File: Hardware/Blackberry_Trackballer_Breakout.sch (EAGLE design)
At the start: 31 parts, among them U1 HALL-EFFECTSMD, U2 HALL-EFFECTSMD, U3 HALL-EFFECTSMD, U4 HALL-EFFECTSMD

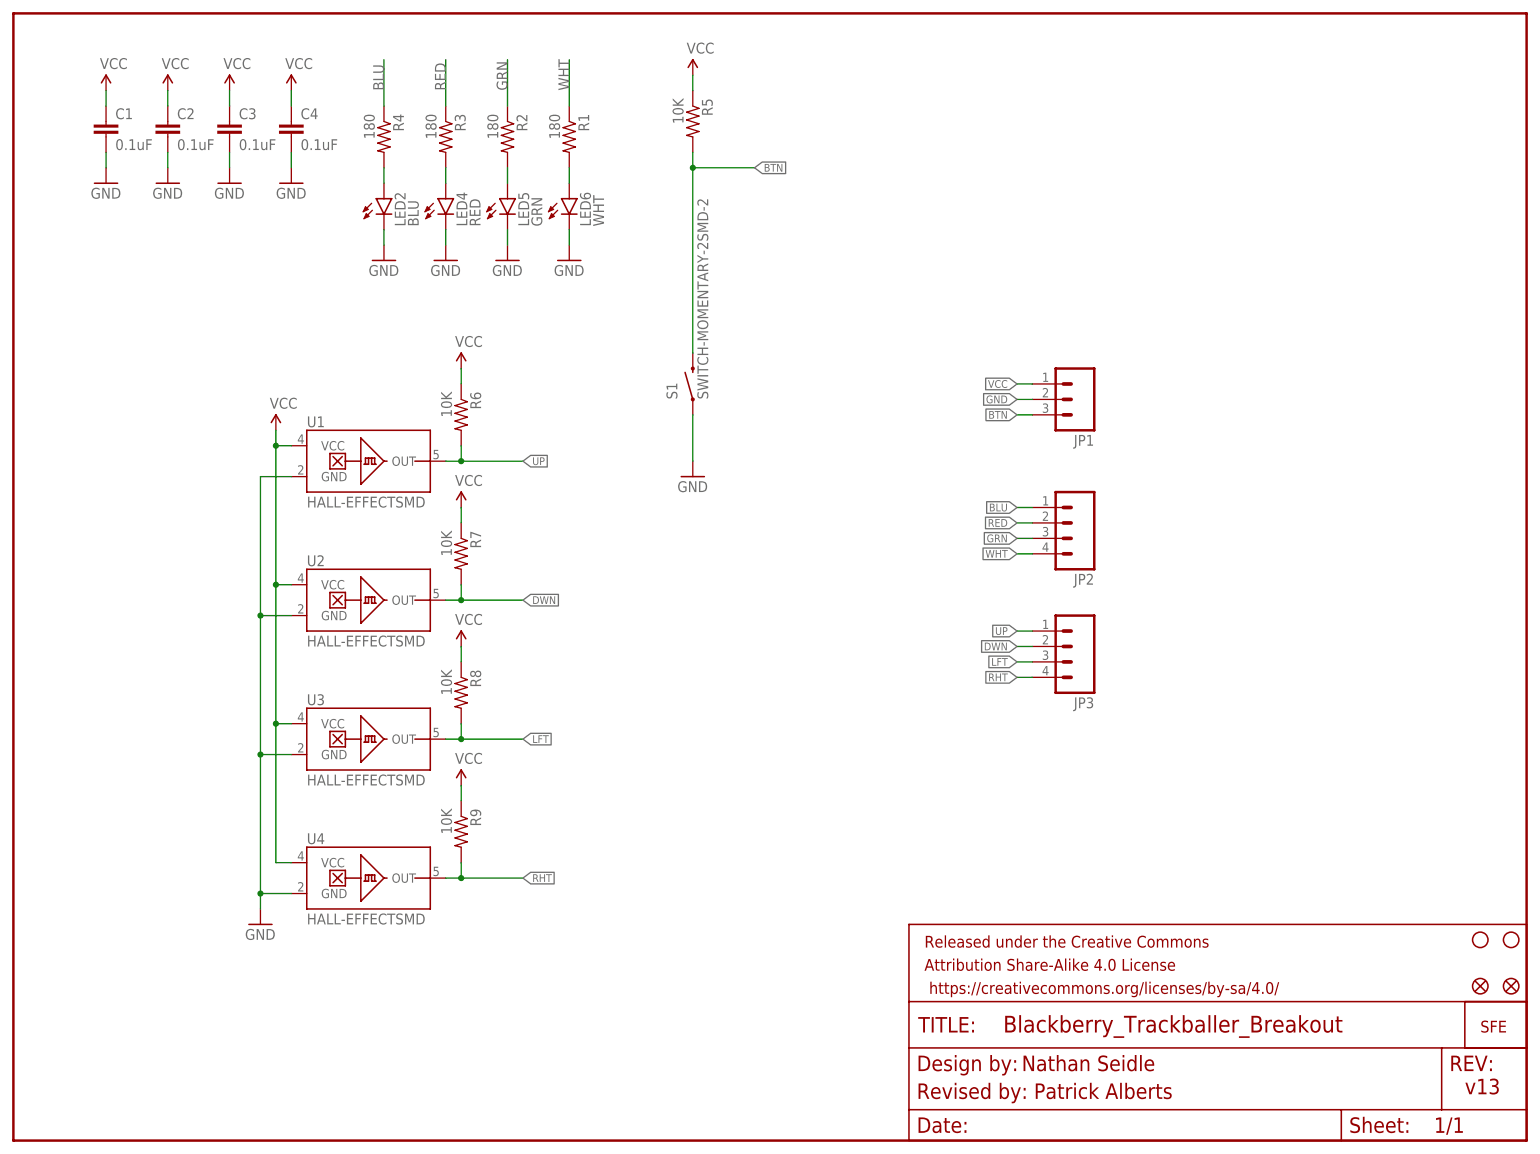
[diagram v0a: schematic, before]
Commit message: initial qc checklist changes.
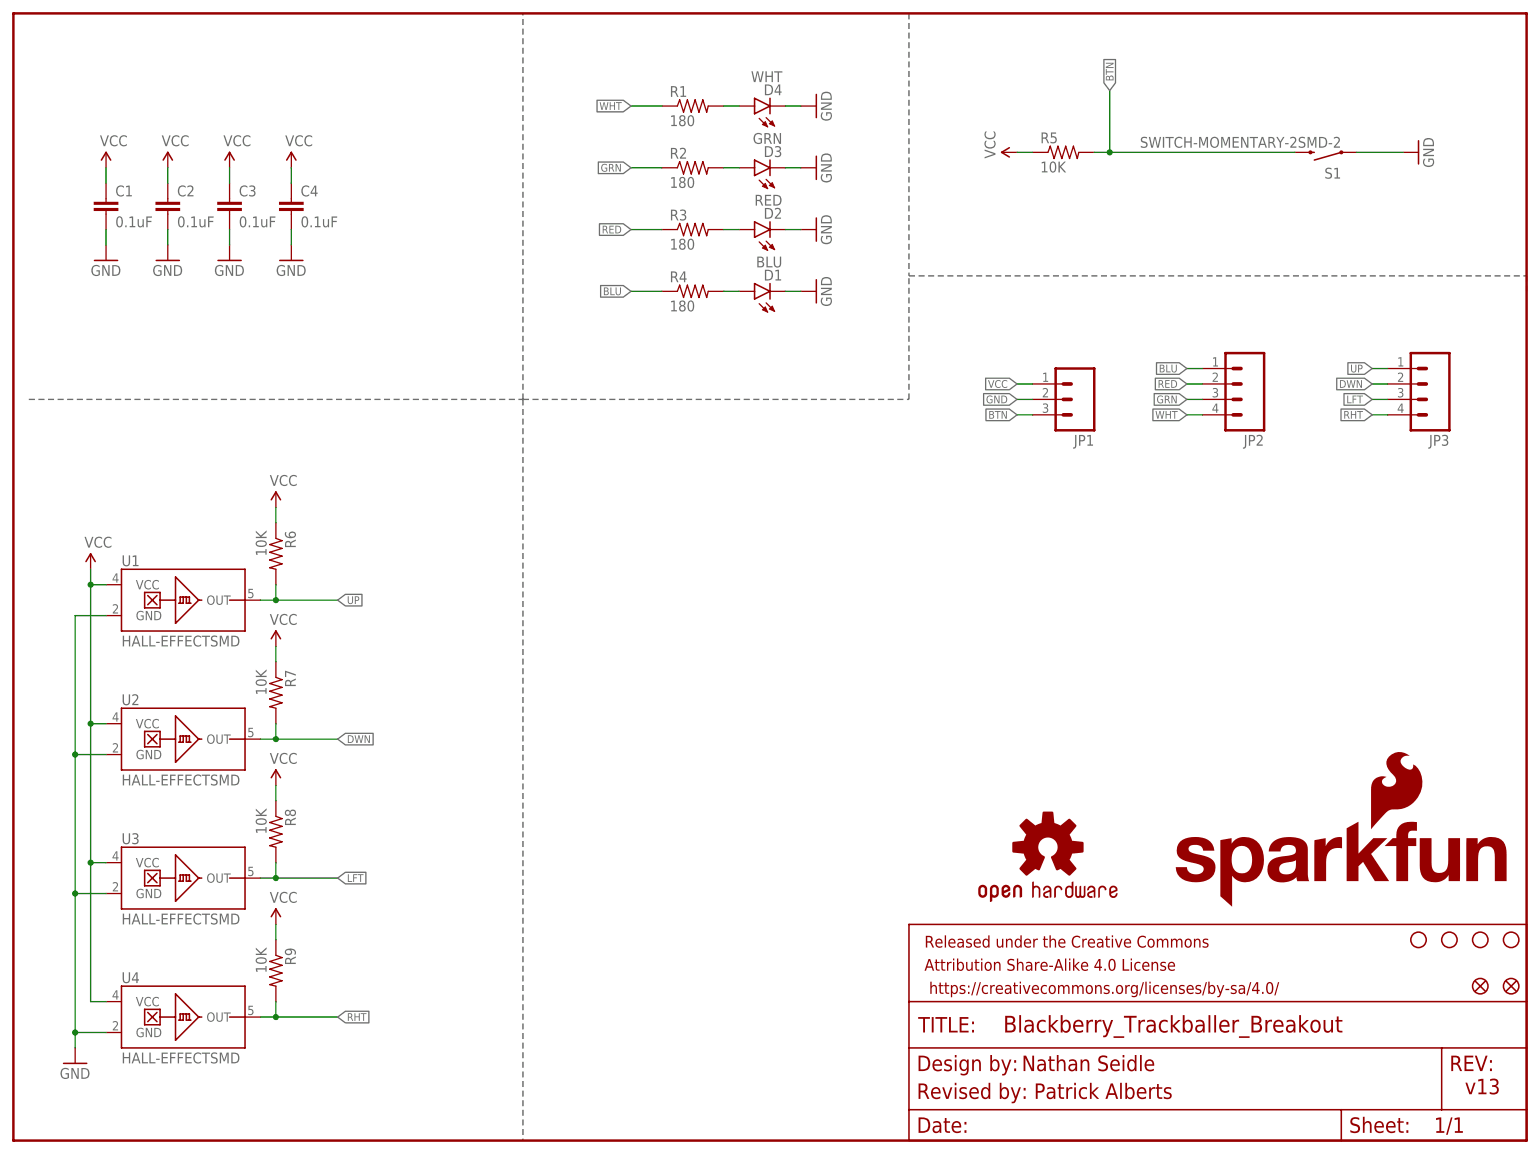
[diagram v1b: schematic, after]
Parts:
- removed LED2: BLU, SparkFun-LED:LED-BLUE0603
- removed LED4: RED, SparkFun-LED:LED-RED0603
- removed LED5: GRN, SparkFun-LED:LED-GREEN0603
- removed LED6: WHT, SparkFun-LED:LED0603
- added D1: BLU, SparkFun-LED:LED-BLUE0603
- added D2: RED, SparkFun-LED:LED-RED0603
- added D3: GRN, SparkFun-LED:LED-GREEN0603
- added D4: WHT, SparkFun-LED:LED0603
- added LOGO1: SFE_LOGO_NAME_FLAME.2_INCH, SparkFun-Aesthetics:SFE_LOGO_NAME_FLAME.2_INCH
- added LOGO2: OSHW-LOGOS, SparkFun-Aesthetics:OSHW-LOGOS
- added U$14: STAND-OFF, SparkFun:STAND-OFF
- U$1: value LOGO-SFENEW -> STAND-OFF; device SparkFun:LOGO-SFENEW -> SparkFun:STAND-OFF
- U1, U2, U3, U4: device SparkFun:HALL-EFFECTSMD -> SparkFun-Sensors:HALL-EFFECTSMD
- renumbered U$9 to U$11
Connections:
- net GND: now also D1.C, D2.C, D3.C, D4.C; no longer LED2.C, LED4.C, LED5.C, LED6.C
- net N$1: now also D3.A; no longer LED5.A
- net N$2: now also D2.A; no longer LED4.A
- net N$3: now also D1.A; no longer LED2.A
- net N$4: now also D4.A; no longer LED6.A
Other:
- moved on the sheet: C1, C2, C3, C4, JP2, JP3, R1, R2, R3, R4, R5, R6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

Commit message: Schematic Clean up, added Blackberry device...
and trace re routes.
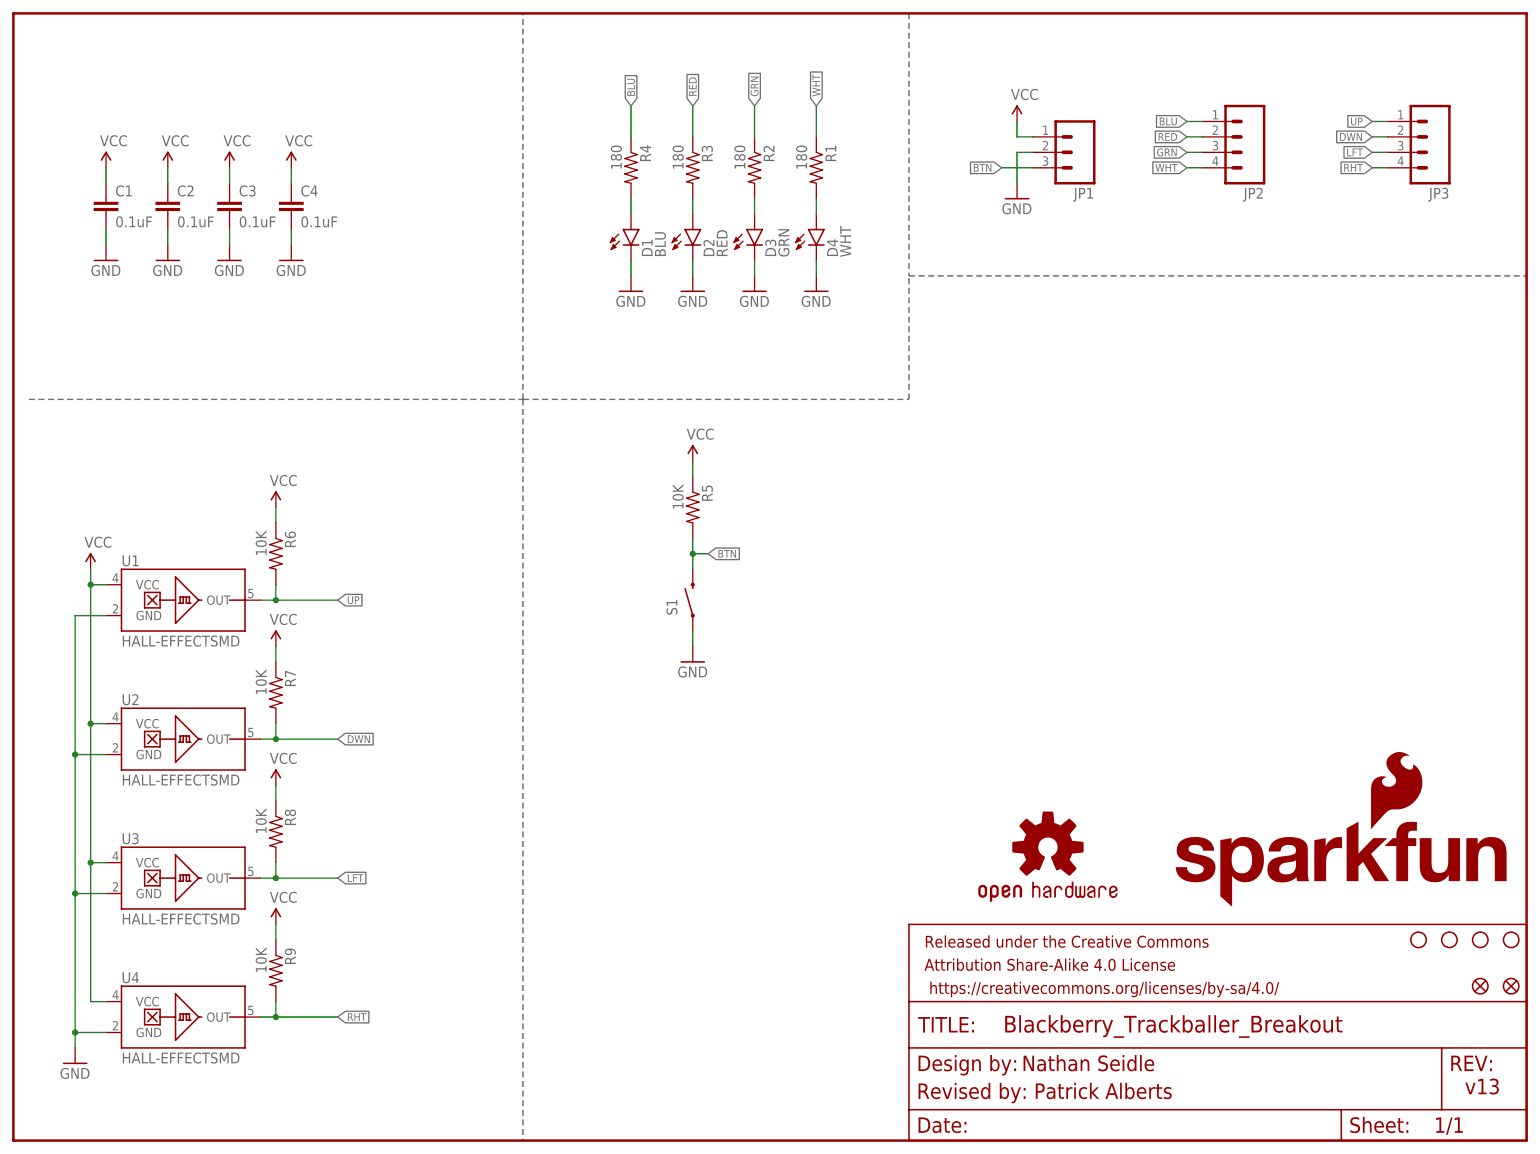
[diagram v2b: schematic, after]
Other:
- moved on the sheet: D1, D2, D3, D4, JP1, JP2, JP3, R1, R2, R3, R4, R5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

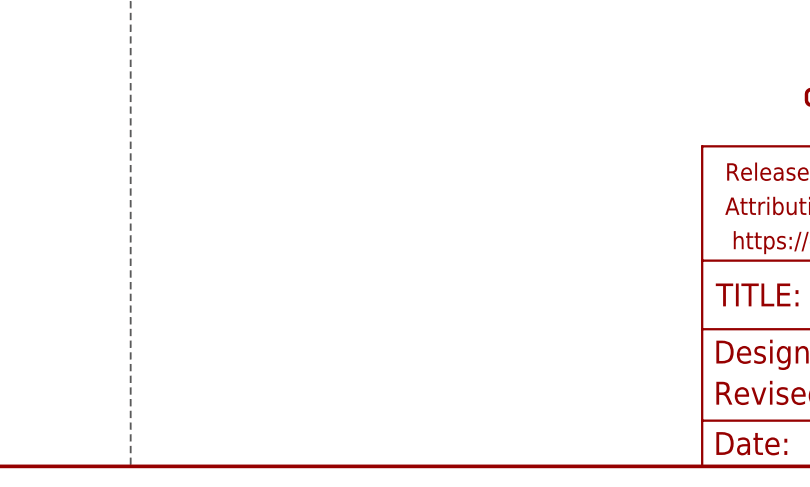
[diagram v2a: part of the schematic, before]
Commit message: Added attributes to swch, trackball and whte led
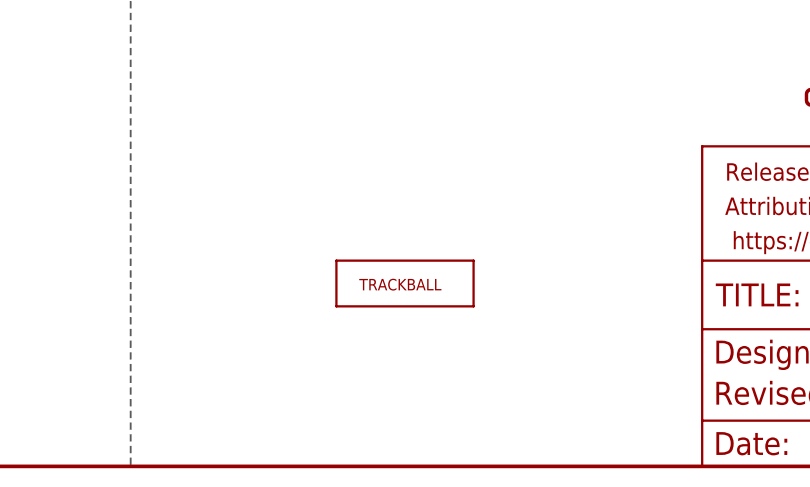
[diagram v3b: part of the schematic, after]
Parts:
- added U$3: TRACKBALLMECH, SparkFun-Electromechanical:TRACKBALLMECH
- D4: device SparkFun-LED:LED0603 -> SparkFun-LED:LED-WHITE0603
- S1: device SparkFun:SWITCH-MOMENTARY-2SMD-2 -> SparkFun-Electromechanical:SWITCH-MOMENTARY-2SMD-2
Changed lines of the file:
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@@
 <part name="E$1" library="SparkFun" deviceset="FIDUCIAL" device="1X2"/>
 <part name="E$2" library="SparkFun" deviceset="FIDUCIAL" device="1X2"/>
-<part name="S1" library="SparkFun" deviceset="SWITCH-MOMENTARY-2" device="SMD-2"/>
+<part name="S1" library="SparkFun-Electromechanical" deviceset="SWITCH-MOMENTARY-2" device="SMD-2"/>
 <part name="D1" library="SparkFun-LED" deviceset="LED-BLUE" device="0603" value="BLU"/>
 <part name="D2" library="SparkFun-LED" deviceset="LED-RED" device="0603" value="RED"/>
 <part name="D3" library="SparkFun-LED" deviceset="LED-GREEN" device="0603" value="GRN"/>
-<part name="D4" library="SparkFun-LED" deviceset="LED" device="0603" value="WHT"/>
+<part name="D4" library="SparkFun-LED" deviceset="LED-WHITE" device="0603" value="WHT"/>
 <part name="U1" library="SparkFun-Sensors" deviceset="HALL-EFFECT" device="SMD"/>
 <part name="P+1" library="SparkFun" deviceset="VCC" device=""/>
@@
 <part name="GND11" library="SparkFun" deviceset="GND" device=""/>
 <part name="P+11" library="SparkFun" deviceset="VCC" device=""/>
+<part name="U$3" library="SparkFun-Electromechanical" deviceset="TRACKBALL" device="MECH"/>
 </parts>
 <sheets>
@@
 <instance part="GND11" gate="1" x="165.1" y="154.94"/>
 <instance part="P+11" gate="1" x="165.1" y="167.64"/>
+<instance part="U$3" gate="G$1" x="114.3" y="20.32"/>
 </instances>
 <busses>

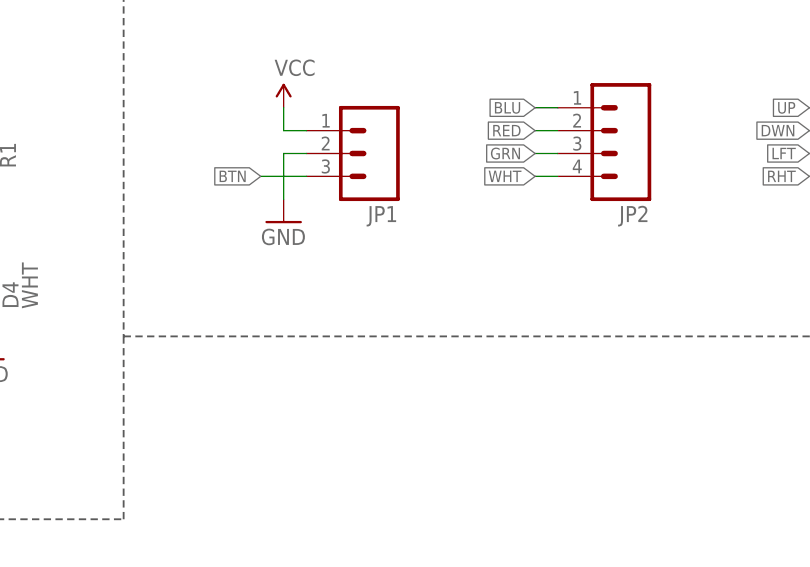
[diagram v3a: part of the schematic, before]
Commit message: Added vcc range to sch
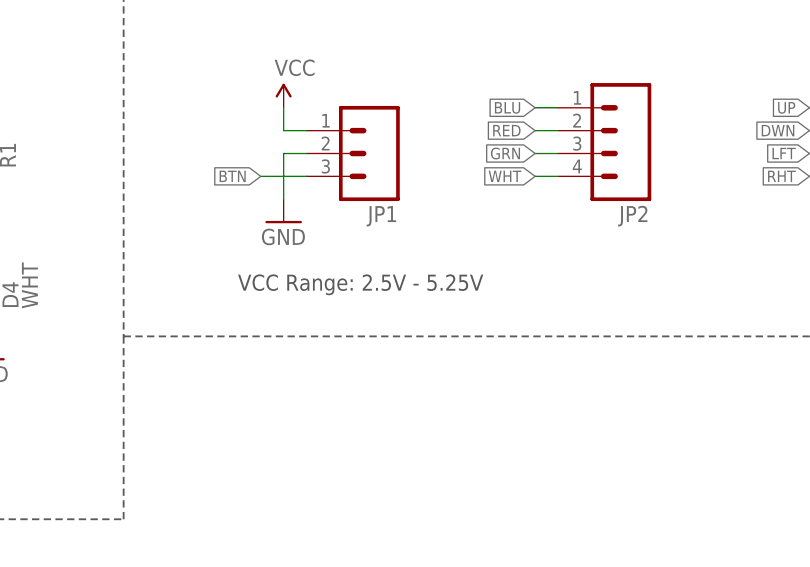
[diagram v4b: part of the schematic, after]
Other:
- note added: "VCC Range: 2.5V - 5.25V"
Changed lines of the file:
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@@
 <wire x1="147.32" y1="142.24" x2="248.92" y2="142.24" width="0.2032" layer="97" style="shortdash"/>
 <wire x1="248.92" y1="142.24" x2="248.92" y2="139.7" width="0.2032" layer="97" style="shortdash"/>
+<text x="160.02" y="147.32" size="1.778" layer="97">VCC Range: 2.5V - 5.25V</text>
 </plain>
 <instances>
